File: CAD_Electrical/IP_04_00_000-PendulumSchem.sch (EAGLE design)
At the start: 5 parts, among them M1 SERVO, M2 SERVO

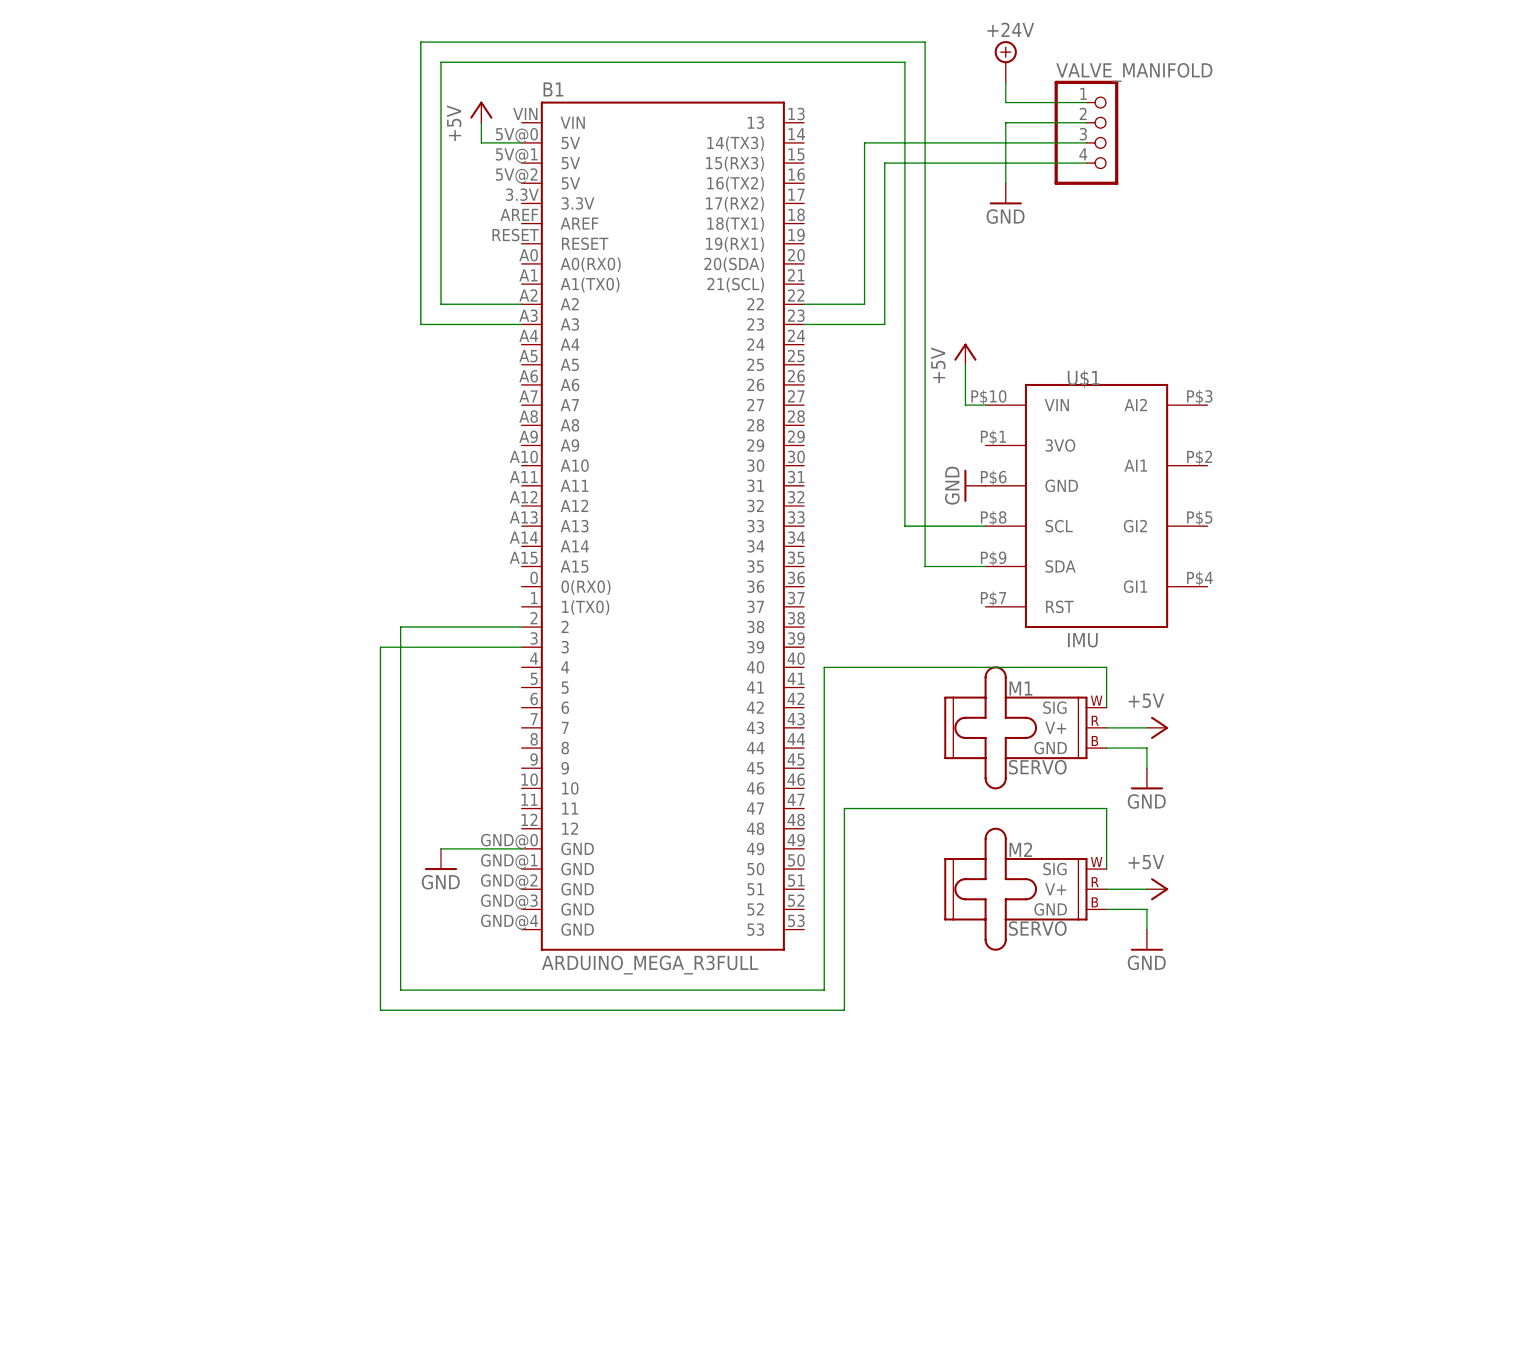
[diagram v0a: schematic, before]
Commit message: Added encoder. Changed IMU wiring to 20 and 21. Fixed valve to digital pwm ports.
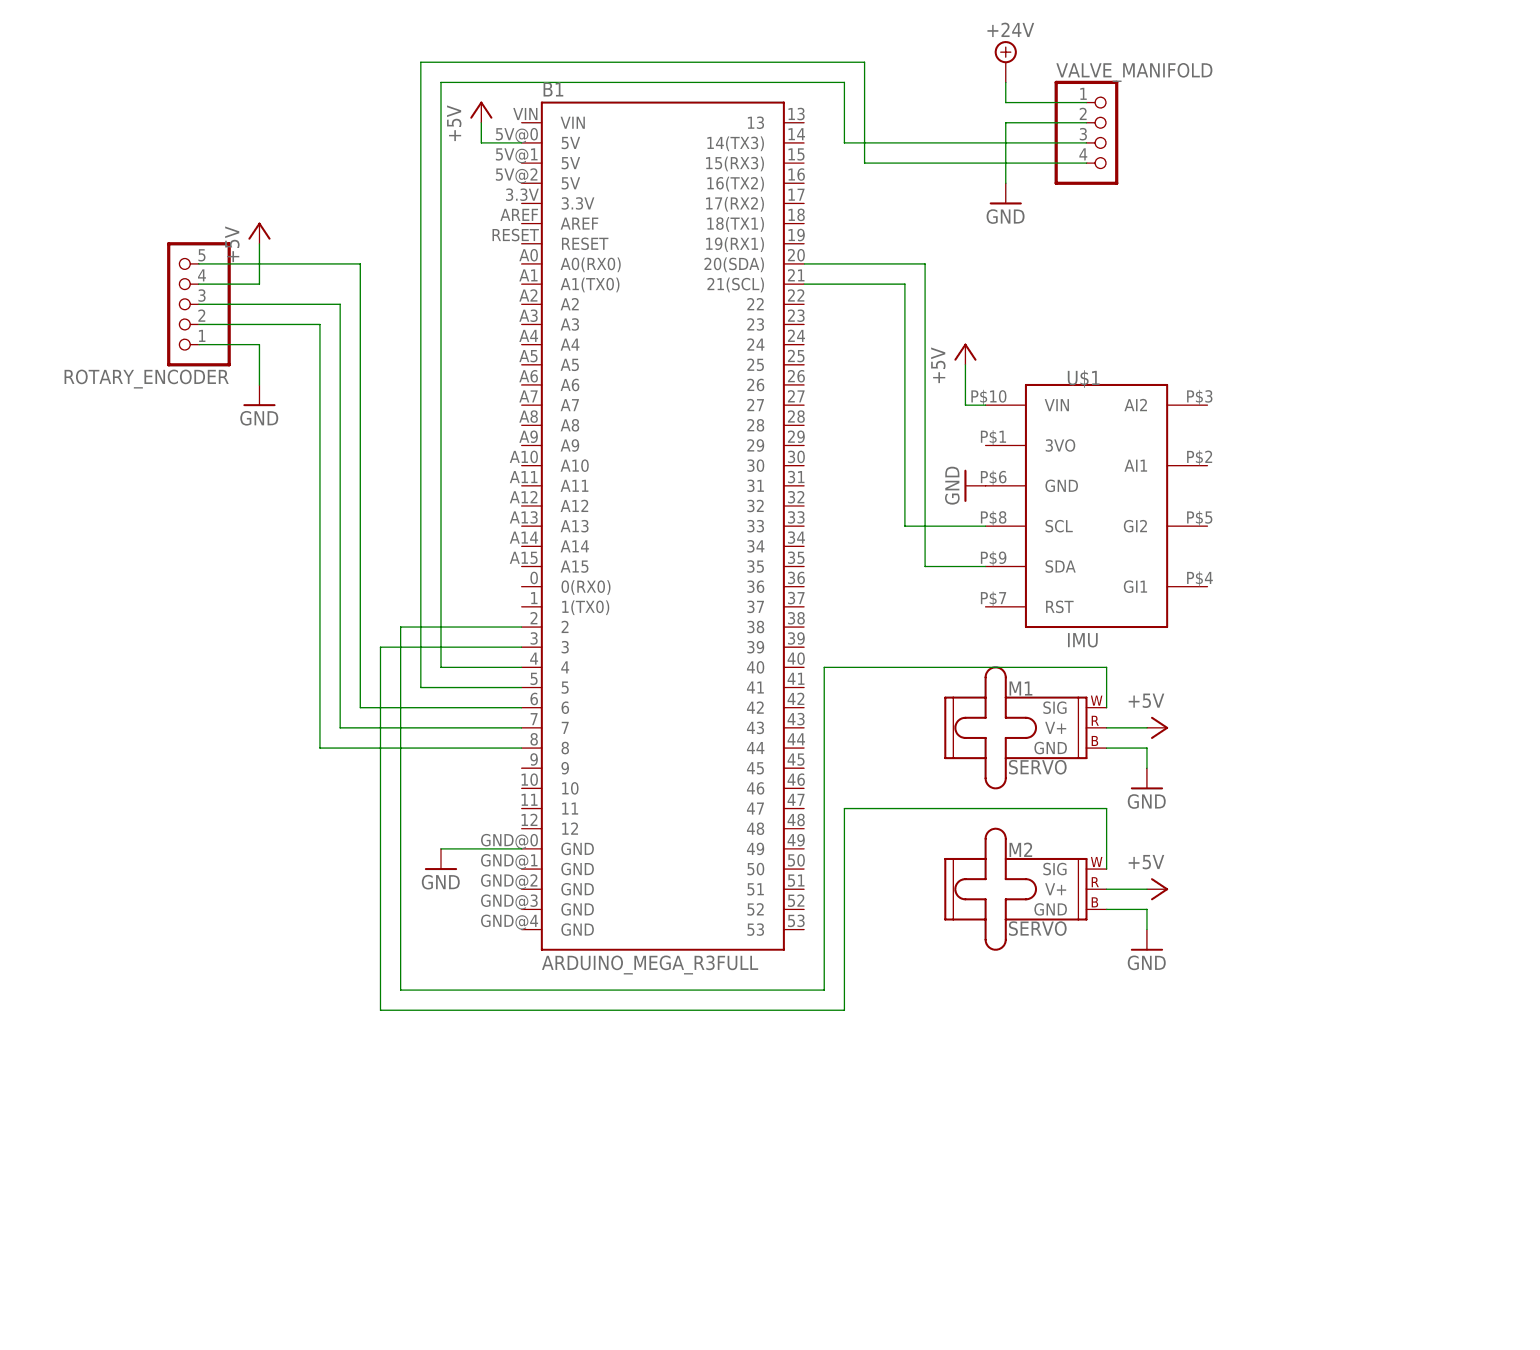
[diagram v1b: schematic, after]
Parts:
- added ROTARY_ENCODER: (no value), pinhead:PINHD-1X5
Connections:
- removed net N$4: B1.A3, U$1.SDA
- new net N$10: B1.7, ROTARY_ENCODER.3
- new net N$11: B1.8, ROTARY_ENCODER.2
- new net N$7: B1.21(SCL), U$1.SCL
- new net N$9: B1.6, ROTARY_ENCODER.5
- net +5V: now also ROTARY_ENCODER.4
- net GND: now also ROTARY_ENCODER.1
- net N$1: now also B1.4; no longer B1.22
- net N$2: now also B1.5; no longer B1.23
- net N$3: now also B1.20(SDA), U$1.SDA; no longer B1.A2, U$1.SCL
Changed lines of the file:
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@@
 <part name="P+3" library="supply1" library_urn="urn:adsk.eagle:library:371" deviceset="+5V" device=""/>
 <part name="P+4" library="supply1" library_urn="urn:adsk.eagle:library:371" deviceset="+5V" device=""/>
+<part name="ROTARY_ENCODER" library="pinhead" library_urn="urn:adsk.eagle:library:325" deviceset="PINHD-1X5" device="" package3d_urn="urn:adsk.eagle:package:22469/2"/>
+<part name="P+5" library="supply1" library_urn="urn:adsk.eagle:library:371" deviceset="+5V" device=""/>
+<part name="GND6" library="supply1" library_urn="urn:adsk.eagle:library:371" deviceset="GND" device=""/>
 </parts>
 <sheets>
@@
 <attribute name="VALUE" x="165.1" y="58.42" size="1.778" layer="96"/>
 </instance>
+<instance part="ROTARY_ENCODER" gate="A" x="45.72" y="129.54" smashed="yes" rot="R180">
+<attribute name="NAME" x="52.07" y="121.285" size="1.778" layer="95" rot="R180"/>
+<attribute name="VALUE" x="52.07" y="139.7" size="1.778" layer="96" rot="R180"/>
+</instance>
+<instance part="P+5" gate="1" x="55.88" y="139.7" smashed="yes">
+<attribute name="VALUE" x="53.34" y="134.62" size="1.778" layer="96" rot="R90"/>
+</instance>
+<instance part="GND6" gate="1" x="55.88" y="116.84" smashed="yes">
+<attribute name="VALUE" x="53.34" y="114.3" size="1.778" layer="96"/>
+</instance>
 </instances>
 <busses>
@@
 <wire x1="167.64" y1="53.34" x2="167.64" y2="50.8" width="0.1524" layer="91"/>
 </segment>
-</net>
-<net name="N$1" class="0">
-<segment>
-<pinref part="VALVE_MANIFOLD" gate="A" pin="3"/>
-<wire x1="160.02" y1="149.86" x2="132.08" y2="149.86" width="0.1524" layer="91"/>
-<wire x1="132.08" y1="149.86" x2="132.08" y2="129.54" width="0.1524" layer="91"/>
-<pinref part="B1" gate="G$1" pin="22"/>
-<wire x1="132.08" y1="129.54" x2="124.46" y2="129.54" width="0.1524" layer="91"/>
-</segment>
-</net>
-<net name="N$2" class="0">
-<segment>
-<pinref part="VALVE_MANIFOLD" gate="A" pin="4"/>
-<wire x1="160.02" y1="147.32" x2="134.62" y2="147.32" width="0.1524" layer="91"/>
-<pinref part="B1" gate="G$1" pin="23"/>
-<wire x1="134.62" y1="147.32" x2="134.62" y2="127" width="0.1524" layer="91"/>
-<wire x1="134.62" y1="127" x2="124.46" y2="127" width="0.1524" layer="91"/>
+<segment>
+<pinref part="ROTARY_ENCODER" gate="A" pin="1"/>
+<wire x1="48.26" y1="124.46" x2="55.88" y2="124.46" width="0.1524" layer="91"/>
+<pinref part="GND6" gate="1" pin="GND"/>
+<wire x1="55.88" y1="124.46" x2="55.88" y2="119.38" width="0.1524" layer="91"/>
 </segment>
 </net>
@@
 <pinref part="M2" gate="G$1" pin="V+"/>
 </segment>
-</net>
-<net name="N$3" class="0">
-<segment>
-<pinref part="U$1" gate="G$1" pin="SCL"/>
-<wire x1="147.32" y1="101.6" x2="137.16" y2="101.6" width="0.1524" layer="91"/>
-<wire x1="137.16" y1="101.6" x2="137.16" y2="160.02" width="0.1524" layer="91"/>
-<wire x1="137.16" y1="160.02" x2="78.74" y2="160.02" width="0.1524" layer="91"/>
-<wire x1="78.74" y1="160.02" x2="78.74" y2="129.54" width="0.1524" layer="91"/>
-<pinref part="B1" gate="G$1" pin="A2"/>
-<wire x1="78.74" y1="129.54" x2="88.9" y2="129.54" width="0.1524" layer="91"/>
-</segment>
-</net>
-<net name="N$4" class="0">
-<segment>
-<pinref part="U$1" gate="G$1" pin="SDA"/>
-<wire x1="147.32" y1="96.52" x2="139.7" y2="96.52" width="0.1524" layer="91"/>
-<wire x1="139.7" y1="96.52" x2="139.7" y2="162.56" width="0.1524" layer="91"/>
-<wire x1="139.7" y1="162.56" x2="76.2" y2="162.56" width="0.1524" layer="91"/>
-<wire x1="76.2" y1="162.56" x2="76.2" y2="127" width="0.1524" layer="91"/>
-<pinref part="B1" gate="G$1" pin="A3"/>
-<wire x1="76.2" y1="127" x2="88.9" y2="127" width="0.1524" layer="91"/>
+<segment>
+<pinref part="ROTARY_ENCODER" gate="A" pin="4"/>
+<wire x1="48.26" y1="132.08" x2="55.88" y2="132.08" width="0.1524" layer="91"/>
+<pinref part="P+5" gate="1" pin="+5V"/>
+<wire x1="55.88" y1="132.08" x2="55.88" y2="137.16" width="0.1524" layer="91"/>
 </segment>
 </net>
@@
 </segment>
 </net>
+<net name="N$7" class="0">
+<segment>
+<pinref part="U$1" gate="G$1" pin="SCL"/>
+<wire x1="147.32" y1="101.6" x2="137.16" y2="101.6" width="0.1524" layer="91"/>
+<wire x1="137.16" y1="101.6" x2="137.16" y2="132.08" width="0.1524" layer="91"/>
+<pinref part="B1" gate="G$1" pin="21(SCL)"/>
+<wire x1="137.16" y1="132.08" x2="124.46" y2="132.08" width="0.1524" layer="91"/>
+</segment>
+</net>
+<net name="N$3" class="0">
+<segment>
+<pinref part="U$1" gate="G$1" pin="SDA"/>
+<wire x1="147.32" y1="96.52" x2="139.7" y2="96.52" width="0.1524" layer="91"/>
+<wire x1="139.7" y1="96.52" x2="139.7" y2="134.62" width="0.1524" layer="91"/>
+<pinref part="B1" gate="G$1" pin="20(SDA)"/>
+<wire x1="139.7" y1="134.62" x2="124.46" y2="134.62" width="0.1524" layer="91"/>
+</segment>
+</net>
+<net name="N$1" class="0">
+<segment>
+<pinref part="VALVE_MANIFOLD" gate="A" pin="3"/>
+<wire x1="160.02" y1="149.86" x2="129.54" y2="149.86" width="0.1524" layer="91"/>
+<wire x1="129.54" y1="149.86" x2="129.54" y2="157.48" width="0.1524" layer="91"/>
+<wire x1="129.54" y1="157.48" x2="78.74" y2="157.48" width="0.1524" layer="91"/>
+<pinref part="B1" gate="G$1" pin="4"/>
+<wire x1="78.74" y1="157.48" x2="78.74" y2="83.82" width="0.1524" layer="91"/>
+<wire x1="78.74" y1="83.82" x2="88.9" y2="83.82" width="0.1524" layer="91"/>
+</segment>
+</net>
+<net name="N$2" class="0">
+<segment>
+<pinref part="VALVE_MANIFOLD" gate="A" pin="4"/>
+<wire x1="160.02" y1="147.32" x2="132.08" y2="147.32" width="0.1524" layer="91"/>
+<wire x1="132.08" y1="147.32" x2="132.08" y2="160.02" width="0.1524" layer="91"/>
+<wire x1="132.08" y1="160.02" x2="76.2" y2="160.02" width="0.1524" layer="91"/>
+<pinref part="B1" gate="G$1" pin="5"/>
+<wire x1="76.2" y1="160.02" x2="76.2" y2="81.28" width="0.1524" layer="91"/>
+<wire x1="76.2" y1="81.28" x2="88.9" y2="81.28" width="0.1524" layer="91"/>
+</segment>
+</net>
+<net name="N$9" class="0">
+<segment>
+<pinref part="ROTARY_ENCODER" gate="A" pin="5"/>
+<wire x1="48.26" y1="134.62" x2="68.58" y2="134.62" width="0.1524" layer="91"/>
+<wire x1="68.58" y1="134.62" x2="68.58" y2="78.74" width="0.1524" layer="91"/>
+<pinref part="B1" gate="G$1" pin="6"/>
+<wire x1="68.58" y1="78.74" x2="88.9" y2="78.74" width="0.1524" layer="91"/>
+</segment>
+</net>
+<net name="N$10" class="0">
+<segment>
+<pinref part="B1" gate="G$1" pin="7"/>
+<wire x1="88.9" y1="76.2" x2="66.04" y2="76.2" width="0.1524" layer="91"/>
+<wire x1="66.04" y1="76.2" x2="66.04" y2="129.54" width="0.1524" layer="91"/>
+<pinref part="ROTARY_ENCODER" gate="A" pin="3"/>
+<wire x1="66.04" y1="129.54" x2="48.26" y2="129.54" width="0.1524" layer="91"/>
+</segment>
+</net>
+<net name="N$11" class="0">
+<segment>
+<pinref part="ROTARY_ENCODER" gate="A" pin="2"/>
+<wire x1="48.26" y1="127" x2="63.5" y2="127" width="0.1524" layer="91"/>
+<wire x1="63.5" y1="127" x2="63.5" y2="73.66" width="0.1524" layer="91"/>
+<pinref part="B1" gate="G$1" pin="8"/>
+<wire x1="63.5" y1="73.66" x2="88.9" y2="73.66" width="0.1524" layer="91"/>
+</segment>
+</net>

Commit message: Inserted transistor array between arduino & valve manifold
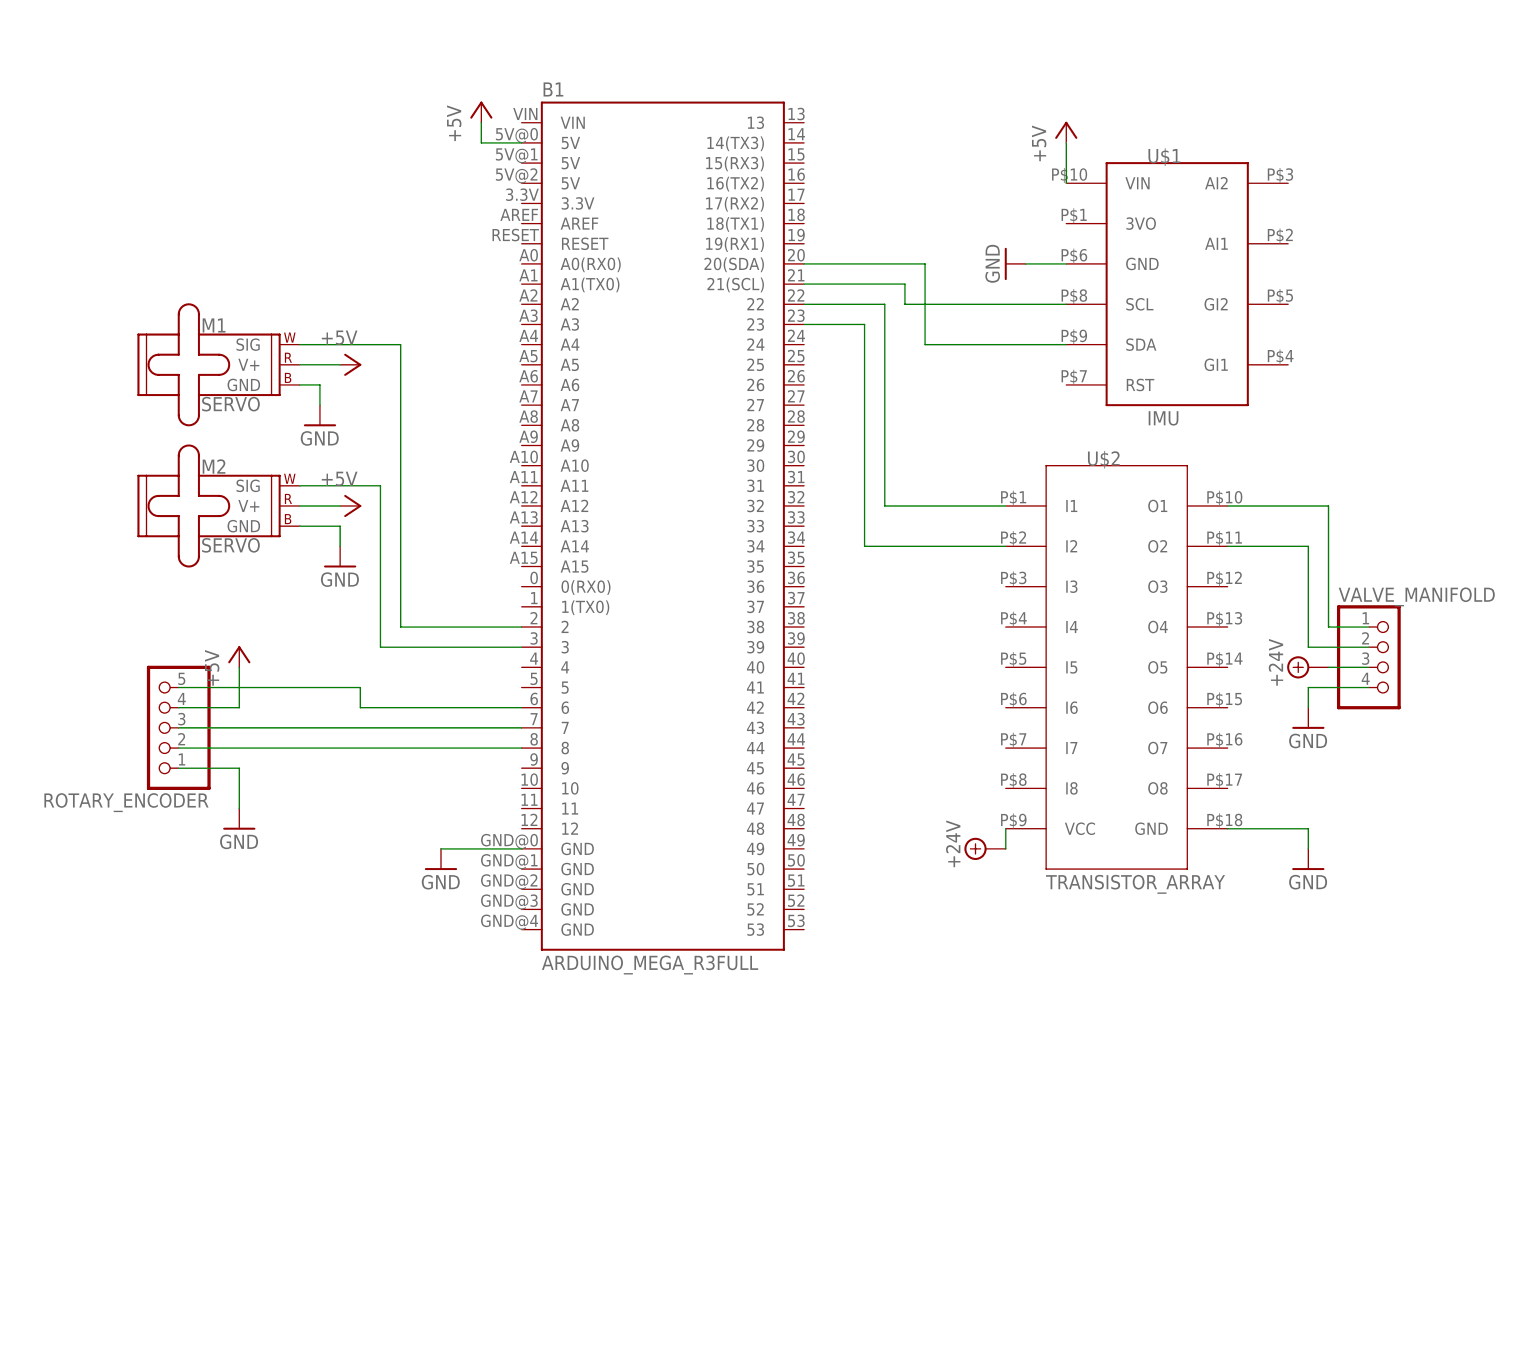
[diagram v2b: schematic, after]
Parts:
- added U$2: TRANSISTOR_ARRAY, IPcustomDevices:TRANSISTOR_ARRAY
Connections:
- removed net N$1 (its old number): B1.4, VALVE_MANIFOLD.3
- removed net N$2 (its old number): B1.5, VALVE_MANIFOLD.4
- new net N$10: B1.23, U$2.I2
- new net N$5: B1.22, U$2.I1
- new net N$6: U$2.O1, VALVE_MANIFOLD.1
- new net N$8: U$2.O2, VALVE_MANIFOLD.2
- net +24V: now also U$2.VCC, VALVE_MANIFOLD.3; no longer VALVE_MANIFOLD.1
- net GND: now also U$2.GND, VALVE_MANIFOLD.4; no longer VALVE_MANIFOLD.2
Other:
- moved on the sheet: M1, M2, ROTARY_ENCODER, U$1, VALVE_MANIFOLD
